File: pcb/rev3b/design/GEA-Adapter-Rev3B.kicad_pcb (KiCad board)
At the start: 4 copper layers, 99 x 40 mm, 99 parts, among them J1 8P8C, J2 RECOVERY, Q3 CJ3407, Q4 CJ3407, Q5 MMBT3904, U10 TPS22810DBVR, U2 XIAO ESP32-C3 v1.3 (22-pad), U4 74LVC2G07, U5 74LVC2G07_3v3, U8 AP63205WU, U9 TPS22810DBVR

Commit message: fix(pcb): connect Rev3B bus input ground return
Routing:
- net GND: vias 10 -> 11
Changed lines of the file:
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@@
+	)
+	(via
+		(at 41 29)
+		(size 0.8)
+		(drill 0.4)
+		(layers "F.Cu" "B.Cu")
+		(net 14)
 	)
 	(via

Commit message: fix(pcb): restore Rev3B bus diode supply connection
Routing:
- net +5V: track 213.9 -> 219.2 mm
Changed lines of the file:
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@@
+	)
+	(segment
+		(start 29.8617 11.3381)
+		(end 28.4499 12.7499)
+		(width 0.5)
+		(layer "F.Cu")
+		(net 2)
 	)
 	(segment
@@
 	)
 	(segment
+		(start 28.4499 12.7499)
+		(end 25.7752 12.7499)
+		(width 0.5)
+		(layer "F.Cu")
+		(net 2)
+	)
+	(segment
 		(start 33.6 27.8983)
 		(end 35.4166 26.0817)
@@
 		(width 0.5)
 		(layer "F.Cu")
+		(net 2)
+	)
+	(segment
+		(start 30.5013 11.3381)
+		(end 29.8617 11.3381)
+		(width 0.5)
+		(layer "F.Cu")

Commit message: fix(pcb): connect Rev3B bus buffer supply
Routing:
- net +5V: track 219.2 -> 229.9 mm
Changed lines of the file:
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@@
+	)
+	(segment
+		(start 31.5324 20.7691)
+		(end 30.092 20.7691)
+		(width 0.5)
+		(layer "F.Cu")
+		(net 2)
+	)
+	(segment
+		(start 33.6875 17.9122)
+		(end 33.6875 19.8104)
+		(width 0.5)
+		(layer "F.Cu")
+		(net 2)
+	)
+	(segment
+		(start 33.6875 19.8104)
+		(end 32.1306 21.3673)
+		(width 0.5)
+		(layer "F.Cu")
+		(net 2)
 	)
 	(segment
@@
 	)
 	(segment
+		(start 31.7753 16)
+		(end 33.6875 17.9122)
+		(width 0.5)
+		(layer "F.Cu")
+		(net 2)
+	)
+	(segment
 		(start 67.7044 1.53)
 		(end 67.7044 6.9363)
@@
 	)
 	(segment
+		(start 30.1375 16)
+		(end 31.7753 16)
+		(width 0.5)
+		(layer "F.Cu")
+		(net 2)
+	)
+	(segment
 		(start 42.4103 5)
 		(end 42.4125 5)
@@
 		(width 0.5)
 		(layer "F.Cu")
+		(net 2)
+	)
+	(segment
+		(start 32.1306 21.3673)
+		(end 31.5324 20.7691)
+		(width 0.5)
+		(layer "F.Cu")

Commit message: fix(pcb): connect Rev3B isolated ground returns
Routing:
- net GND: vias 11 -> 16
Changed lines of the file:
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@@
+	)
+	(via
+		(at 28.007 5.507)
+		(size 0.8)
+		(drill 0.4)
+		(layers "F.Cu" "B.Cu")
+		(net 14)
+	)
+	(via
+		(at 56.12 22.507)
+		(size 0.8)
+		(drill 0.4)
+		(layers "F.Cu" "B.Cu")
+		(net 14)
+	)
+	(via
+		(at 28.031 22.557)
+		(size 0.8)
+		(drill 0.4)
+		(layers "F.Cu" "B.Cu")
+		(net 14)
 	)
 	(via
@@
 	)
 	(via
+		(at 62.93 24.42)
+		(size 0.8)
+		(drill 0.4)
+		(layers "F.Cu" "B.Cu")
+		(net 14)
+	)
+	(via
 		(at 67.9 24)
 		(size 0.8)
 		(drill 0.4)
+		(layers "F.Cu" "B.Cu")
+		(net 14)
+	)
+	(via
+		(at 51.04 22.493)
+		(size 0.8)
+		(drill 0.4)

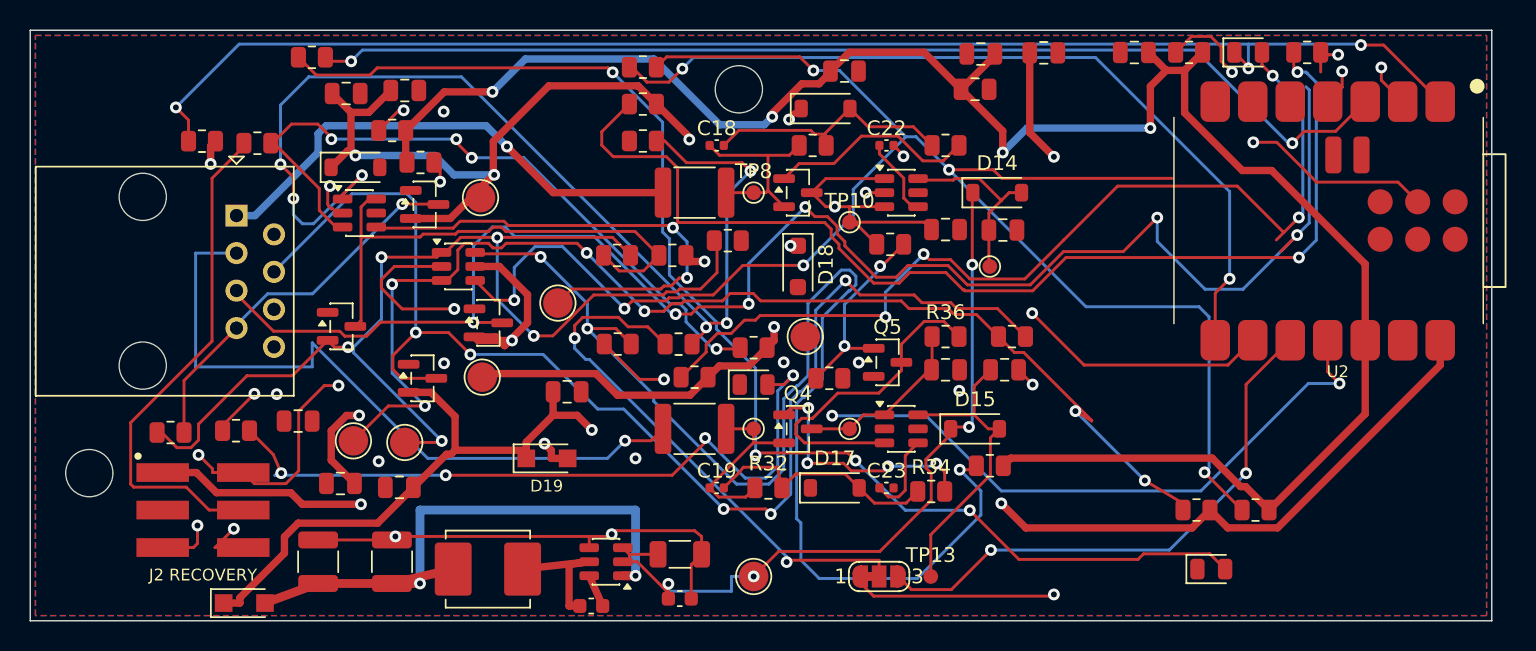
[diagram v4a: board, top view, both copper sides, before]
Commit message: refactor(pcb): arrange Rev3B four-layer functional blocks
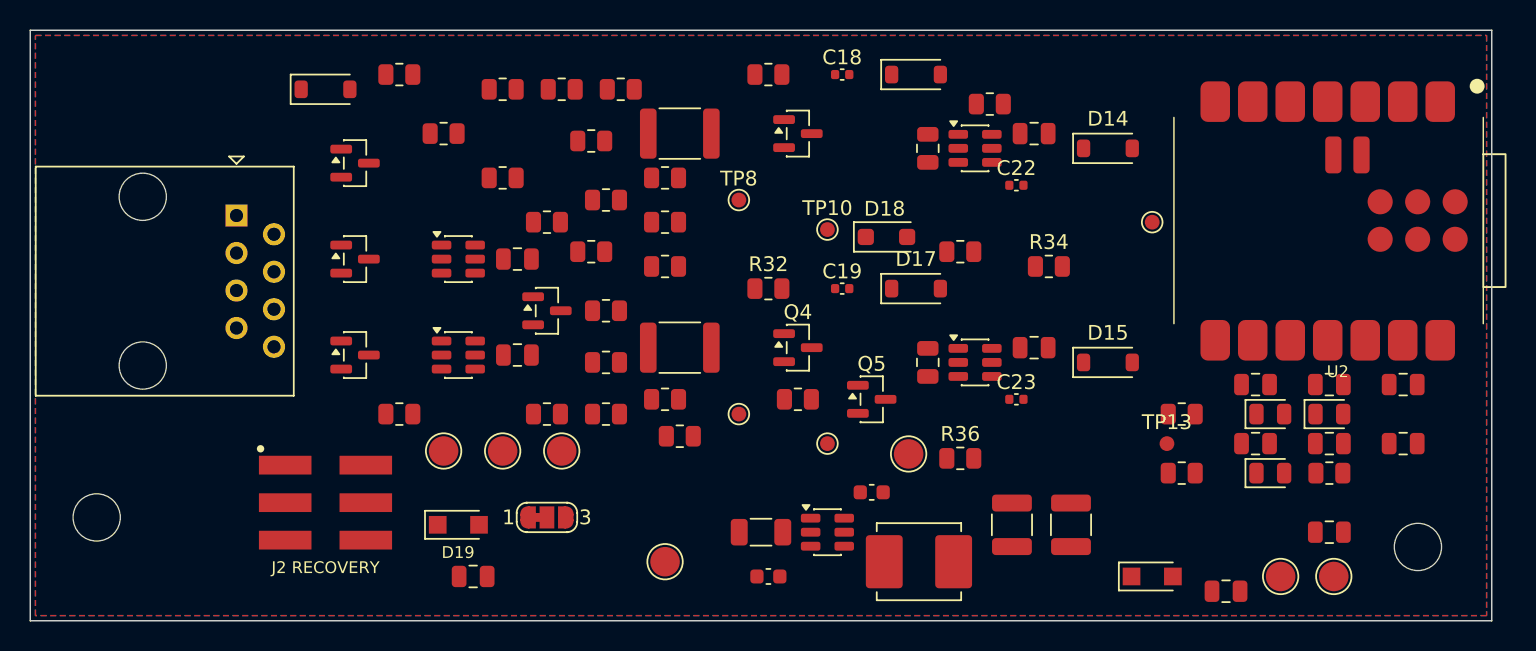
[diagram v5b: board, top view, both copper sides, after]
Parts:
- moved R7 74.5 mm to (88.0, 30.0)
- moved C3 69.5 mm to (88.0, 24.0)
- moved C5 64.9 mm to (83.0, 28.0)
- moved R6 64.1 mm to (78.0, 30.0)
- moved D11 61.5 mm to (76.0, 37.0)
- moved TP1 60.0 mm to (84.7, 37.0)
- moved TP2 59.2 mm to (88.3, 37.0)
- moved H2 55.5 mm to (94.0, 35.0)
- moved C17 51.1 mm to (70.5, 33.5)
- moved R24 48.9 mm to (38.0, 7.50)
- moved C11 46.6 mm to (81.0, 38.0)
- moved R17 45.9 mm to (43.0, 10.0)
- moved C13 43.4 mm to (93.0, 24.0)
- moved R3 42.6 mm to (36.0, 4.00)
- moved C16 42.1 mm to (66.5, 33.5)
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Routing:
- net +5V: track 229.9 -> 0.00 mm, vias 8 -> 0
- net +3V3: track 227.5 -> 0.00 mm, vias 7 -> 0
- net BOOT: track 129.6 -> 0.00 mm, vias 5 -> 0
- net GEA_FullRx: track 126.2 -> 0.00 mm, vias 7 -> 0
- net /LED2: track 125.5 -> 0.00 mm, vias 2 -> 0
- net EN: track 120.9 -> 0.00 mm, vias 3 -> 0
- net Net-(R13-Pad2): track 114.8 -> 0.00 mm, vias 6 -> 0
- net Net-(R20-Pad1): track 108.7 -> 0.00 mm, vias 4 -> 0
- net GEA3_TX: track 104.6 -> 0.00 mm, vias 3 -> 0
- net /DBG_LED: track 94.8 -> 0.00 mm, vias 3 -> 0
- net Net-(R10-Pad2): track 89.3 -> 0.00 mm, vias 3 -> 0
- net GEA_FullTx: track 88.1 -> 0.00 mm, vias 5 -> 0
- net Net-(D6-A): track 87.5 -> 0.00 mm, vias 4 -> 0
- net Net-(R21-Pad1): track 82.0 -> 0.00 mm, vias 6 -> 0
- net Net-(D9-K2): track 77.9 -> 0.00 mm, vias 5 -> 0
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
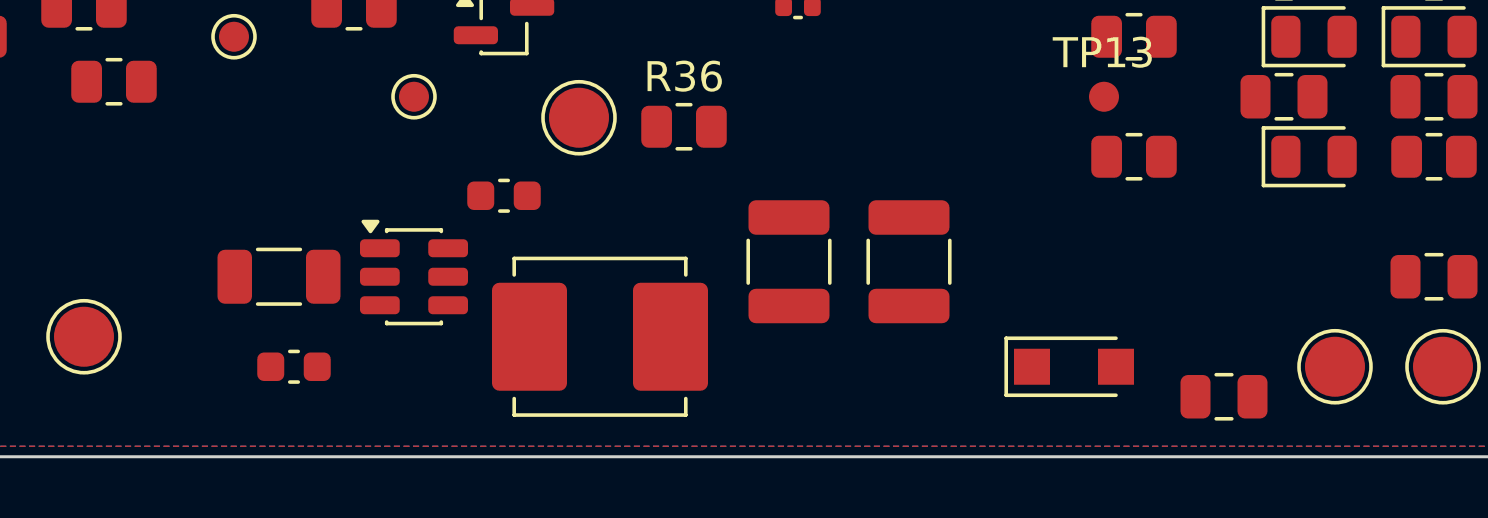
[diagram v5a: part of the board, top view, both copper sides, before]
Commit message: feat(pcb): route Rev3B local buck supply
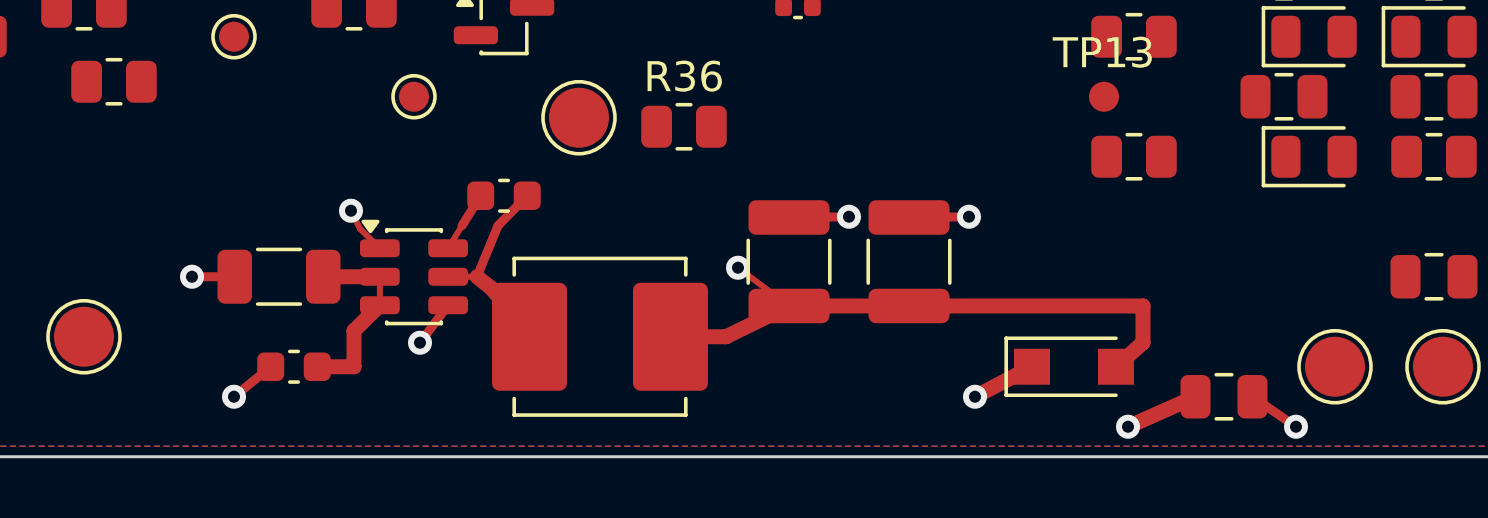
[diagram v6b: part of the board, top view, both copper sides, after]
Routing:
- net /BUCK_5V: track 0.00 -> 36.9 mm, vias 0 -> 2
- net GND: track 0.00 -> 10.3 mm, vias 0 -> 6
- net +5V: track 0.00 -> 9.81 mm, vias 0 -> 2
- net /BUCK_SW: track 0.00 -> 6.87 mm
- net /V_INPUT: track 0.00 -> 6.47 mm
- net /BUCK_BST: track 0.00 -> 2.06 mm

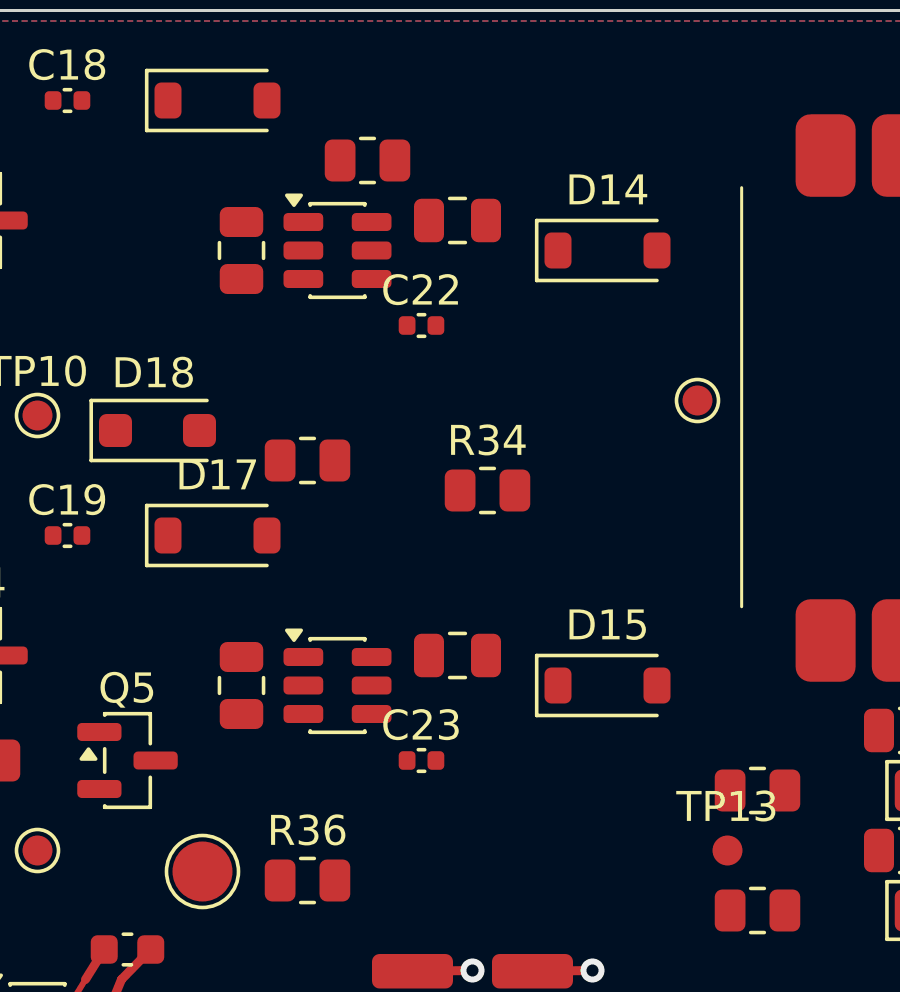
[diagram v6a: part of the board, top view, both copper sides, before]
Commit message: feat(pcb): route Rev3B local input selectors
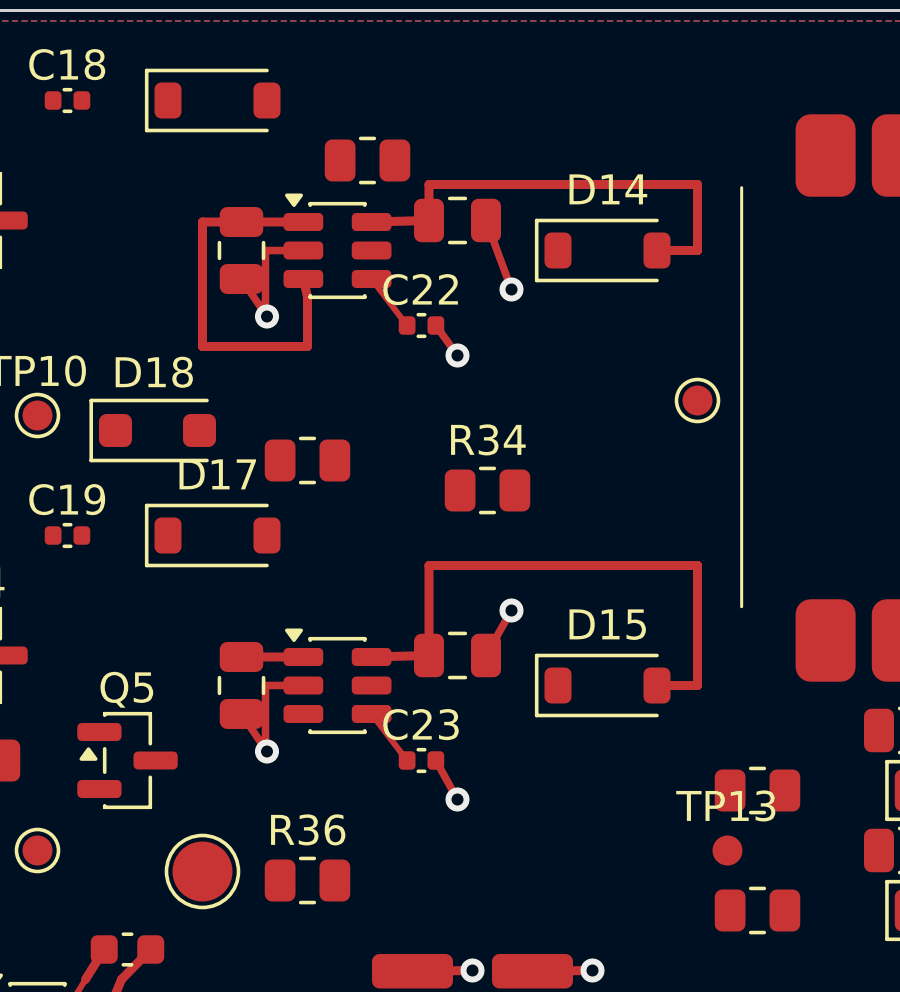
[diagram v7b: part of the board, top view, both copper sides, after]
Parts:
- turned C20 to -90 degrees
- turned C21 to -90 degrees
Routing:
- net /PIN3_SW_OUT: track 0.00 -> 19.2 mm
- net GND: track 10.3 -> 27.3 mm, vias 6 -> 12
- net /PIN1_SW_OUT: track 0.00 -> 15.6 mm
- net /PIN1_PROTECTED: track 0.00 -> 13.3 mm
- net /PIN3_PROTECTED: track 0.00 -> 2.06 mm
- net /PIN3_CT: track 0.00 -> 1.95 mm
- net /PIN1_CT: track 0.00 -> 1.95 mm
